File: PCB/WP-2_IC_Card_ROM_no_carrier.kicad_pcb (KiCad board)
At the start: 2 copper layers, 45 x 54 mm, 5 parts, among them J1 Conn_01x38_Female, U1 FLASH 256Kx8 5v Parallel, U2 FLASH 256Kx8 5v Parallel

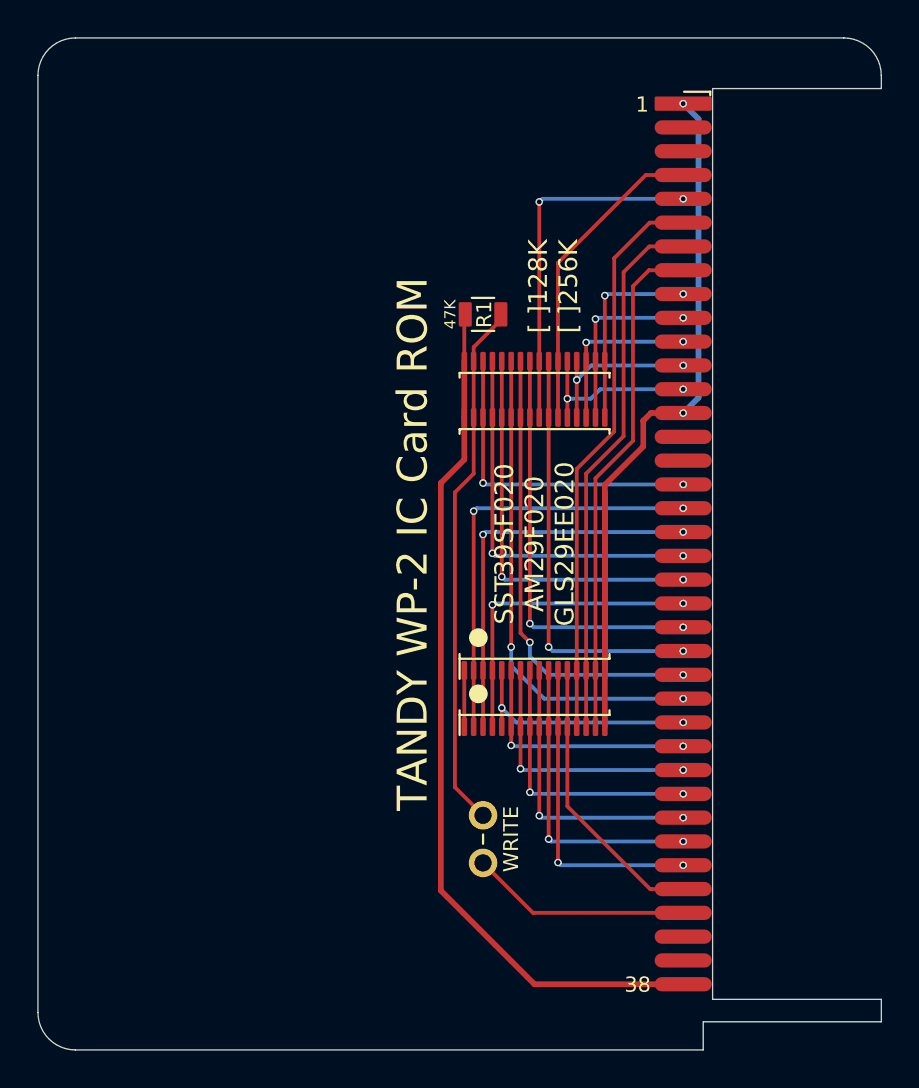
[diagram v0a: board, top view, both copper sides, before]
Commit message: fix ROM flash chip pinout
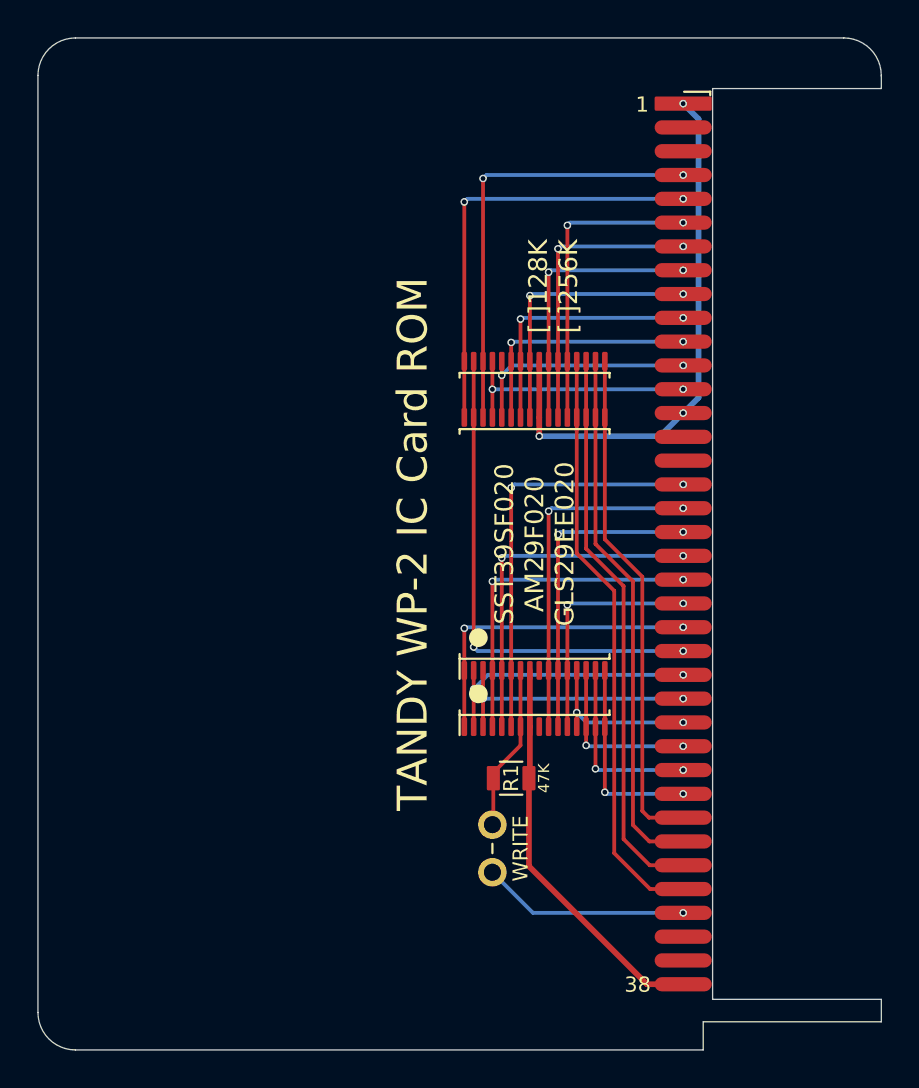
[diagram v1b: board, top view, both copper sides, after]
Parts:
- JP1: value WR_EN -> Write-Enable
- moved R1 24.8 mm to (148.0, 112.2), turned to 180 degrees
- moved JP1 0.71 mm to (147.0, 115.9)
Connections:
- U1 pad 1: (no net) -> /A11
- U1 pad 10: /A2 -> /A16
- U1 pad 11: /A1 -> /A15
- U1 pad 12: /A0 -> /A12
- U1 pad 13: /D0 -> /A7
- U1 pad 14: /D1 -> /A6
- U1 pad 15: /D2 -> /A5
- U1 pad 16: GND -> /A4
- U1 pad 17: /D3 -> /A3
- U1 pad 18: /D4 -> /A2
- U1 pad 19: /D5 -> /A1
- U1 pad 2: /A16 -> /A9
- U1 pad 20: /D6 -> /A0
- U1 pad 21: /D7 -> /D0
- U1 pad 22: /~CE1 -> /D1
- U1 pad 23: /A10 -> /D2
- U1 pad 24: /~OE -> GND
- U1 pad 25: /A11 -> /D3
- U1 pad 26: /A9 -> /D4
- U1 pad 27: /A8 -> /D5
- U1 pad 28: /A13 -> /D6
- U1 pad 29: /A14 -> /D7
- U1 pad 3: /A15 -> /A8
- U1 pad 30: /A17 -> /~CE1
- U1 pad 31: /~WE -> /A10
- U1 pad 32: VDD -> /~OE
- U1 pad 4: /A12 -> /A13
- U1 pad 5: /A7 -> /A14
- U1 pad 6: /A6 -> /A17
- U1 pad 7: /A5 -> /~WE
- U1 pad 8: /A4 -> VDD
- U1 pad 9: /A3 -> (no net)
- U2 pad 1: (no net) -> /A11
- U2 pad 10: /A2 -> /A16
- U2 pad 11: /A1 -> /A15
- U2 pad 12: /A0 -> /A12
- U2 pad 13: /D0 -> /A7
- U2 pad 14: /D1 -> /A6
- U2 pad 15: /D2 -> /A5
- U2 pad 16: GND -> /A4
- U2 pad 17: /D3 -> /A3
- U2 pad 18: /D4 -> /A2
- U2 pad 19: /D5 -> /A1
- U2 pad 2: /A16 -> /A9
- U2 pad 20: /D6 -> /A0
- U2 pad 21: /D7 -> /D0
- U2 pad 22: /~CE1 -> /D1
- U2 pad 23: /A10 -> /D2
- U2 pad 24: /~OE -> GND
- U2 pad 25: /A11 -> /D3
- U2 pad 26: /A9 -> /D4
- U2 pad 27: /A8 -> /D5
- U2 pad 28: /A13 -> /D6
- U2 pad 29: /A14 -> /D7
- U2 pad 3: /A15 -> /A8
- U2 pad 30: /A17 -> /~CE1
- U2 pad 31: /~WE -> /A10
- U2 pad 32: VDD -> /~OE
- U2 pad 4: /A12 -> /A13
- U2 pad 5: /A7 -> /A14
- U2 pad 6: /A6 -> /A17
- U2 pad 7: /A5 -> /~WE
- U2 pad 8: /A4 -> VDD
- U2 pad 9: /A3 -> (no net)
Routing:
- net VDD: track 46.3 -> 21.3 mm
- net /~WE: track 28.4 -> 8.85 mm
- net GND: track 46.2 -> 29.4 mm, vias 2 -> 3
- net /A0: track 15.3 -> 31.6 mm
- net /D0: track 30.3 -> 16.5 mm, vias 0 -> 2
- net /A1: track 17.0 -> 30.1 mm, vias 2 -> 0
- net /D1: track 28.8 -> 15.7 mm, vias 0 -> 2
- net /A8: track 26.2 -> 13.7 mm
- net /D2: track 27.4 -> 15.0 mm, vias 0 -> 2
- net /A2: track 16.2 -> 28.6 mm, vias 2 -> 0
- net /A3: track 15.5 -> 27.2 mm, vias 2 -> 0
- net /A9: track 24.5 -> 14.5 mm
- net /~CE1: track 16.9 -> 23.5 mm, vias 0 -> 2
- net /A11: track 22.3 -> 17.0 mm
- net /A17: track 17.2 -> 22.0 mm
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
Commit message: fine-tune via-near-trace placements
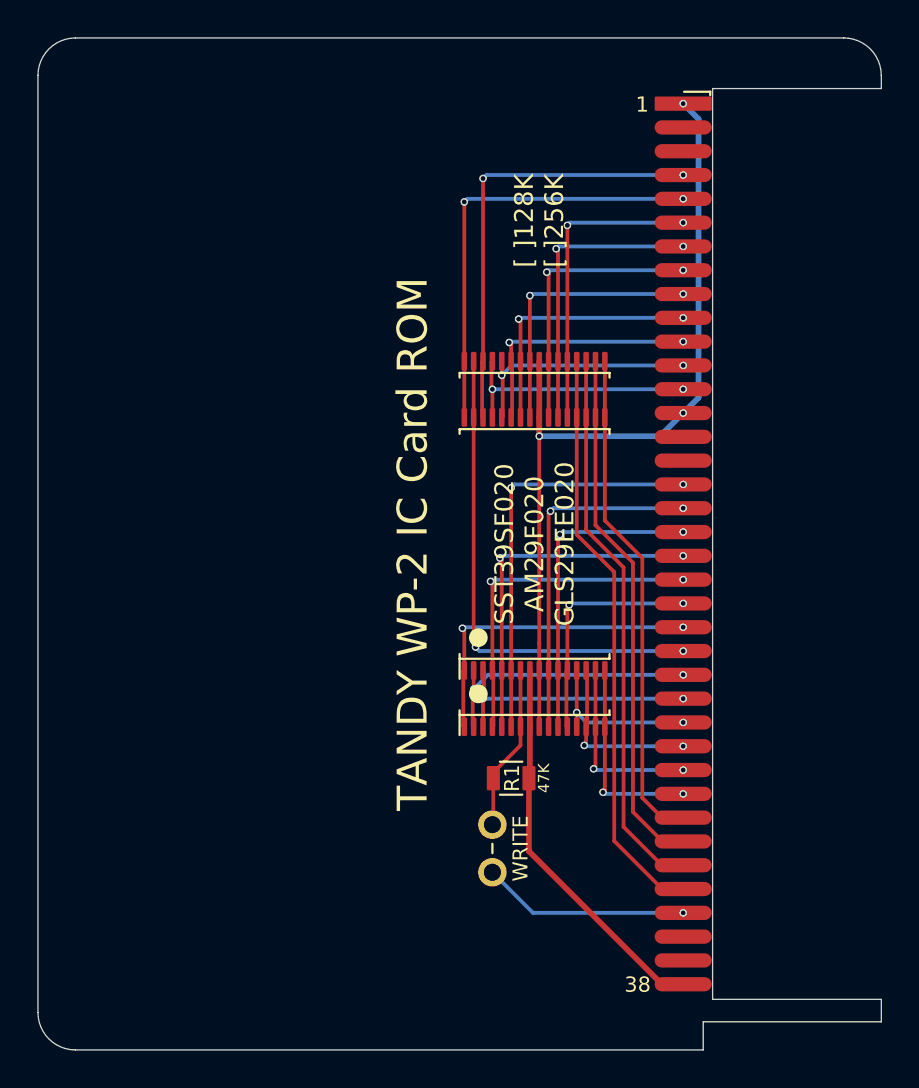
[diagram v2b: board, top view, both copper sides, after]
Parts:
- added NT1: Net-Tie_2, 0_LOCAL:Net_Tie_2p_8mil, F.Cu at (149.5, 105.2)
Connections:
- U1 pad 9: (no net) -> /A18
- U2 pad 9: (no net) -> /A18
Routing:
- net GND: track 29.4 -> 40.5 mm
- net /A18: track 0.00 -> 4.05 mm

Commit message: increase via sizes and min soldermask width for PCBWAY
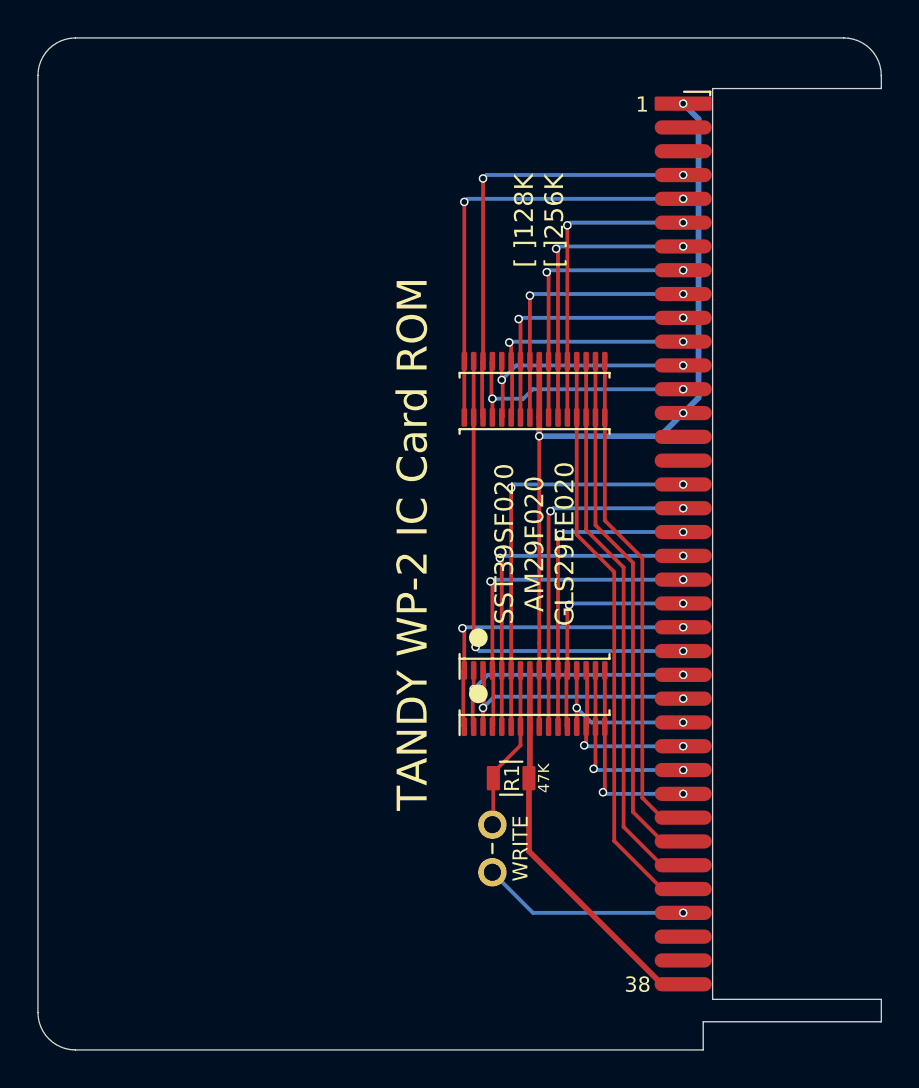
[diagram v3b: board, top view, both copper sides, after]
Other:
- net class Default: via_dia 0.4064 -> 0.46; via_drill 0.254 -> 0.3
- rule via_min_drill: 0.254 -> 0.3
- rule via_min_size: 0.4064 -> 0.46
